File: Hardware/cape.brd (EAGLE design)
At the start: 105 x 118 mm, 99 parts, among them IC1 RT7258, IC2 RT7258, IC3 74HC125, J1 JST-BM07B-GHS-TBT, J10 JST-BM07B-GHS-TBT, J11 JST-BM07B-GHS-TBT, J12 JST-BM07B-GHS-TBT, J13 JST-BM07B-GHS-TBT, J14 JST-BM07B-GHS-TBT, J15 JST-BM07B-GHS-TBT, J16 JST-BM07B-GHS-TBT, J17 JST-BM07B-GHS-TBT, J18 JST-BM07B-GHS-TBT, J19 JST-BM07B-GHS-TBT, J2 JST-BM07B-GHS-TBT, J20 JST-BM07B-GHS-TBT, J21 JST-BM07B-GHS-TBT, J22 JST-BM07B-GHS-TBT, J23 JST-BM07B-GHS-TBT, J24 JST-BM07B-GHS-TBT, J25 JST-BM07B-GHS-TBT, J26 JST-BM07B-GHS-TBT, J27 JST-BM07B-GHS-TBT, J28 JST-BM07B-GHS-TBT, J29 JST-BM07B-GHS-TBT, J3 JST-BM07B-GHS-TBT, J30 JST-BM07B-GHS-TBT, J31 JST-BM07B-GHS-TBT, J32 JST-BM07B-GHS-TBT, J4 JST-BM07B-GHS-TBT, J5 JST-BM07B-GHS-TBT, J6 JST-BM07B-GHS-TBT, J7 JST-BM07B-GHS-TBT, J8 JST-BM07B-GHS-TBT, J9 JST-BM07B-GHS-TBT, Q1 FDS6670, Q2 FDS6670, X1 RJ45-6L2-B, X2 RJ45-6L2-B

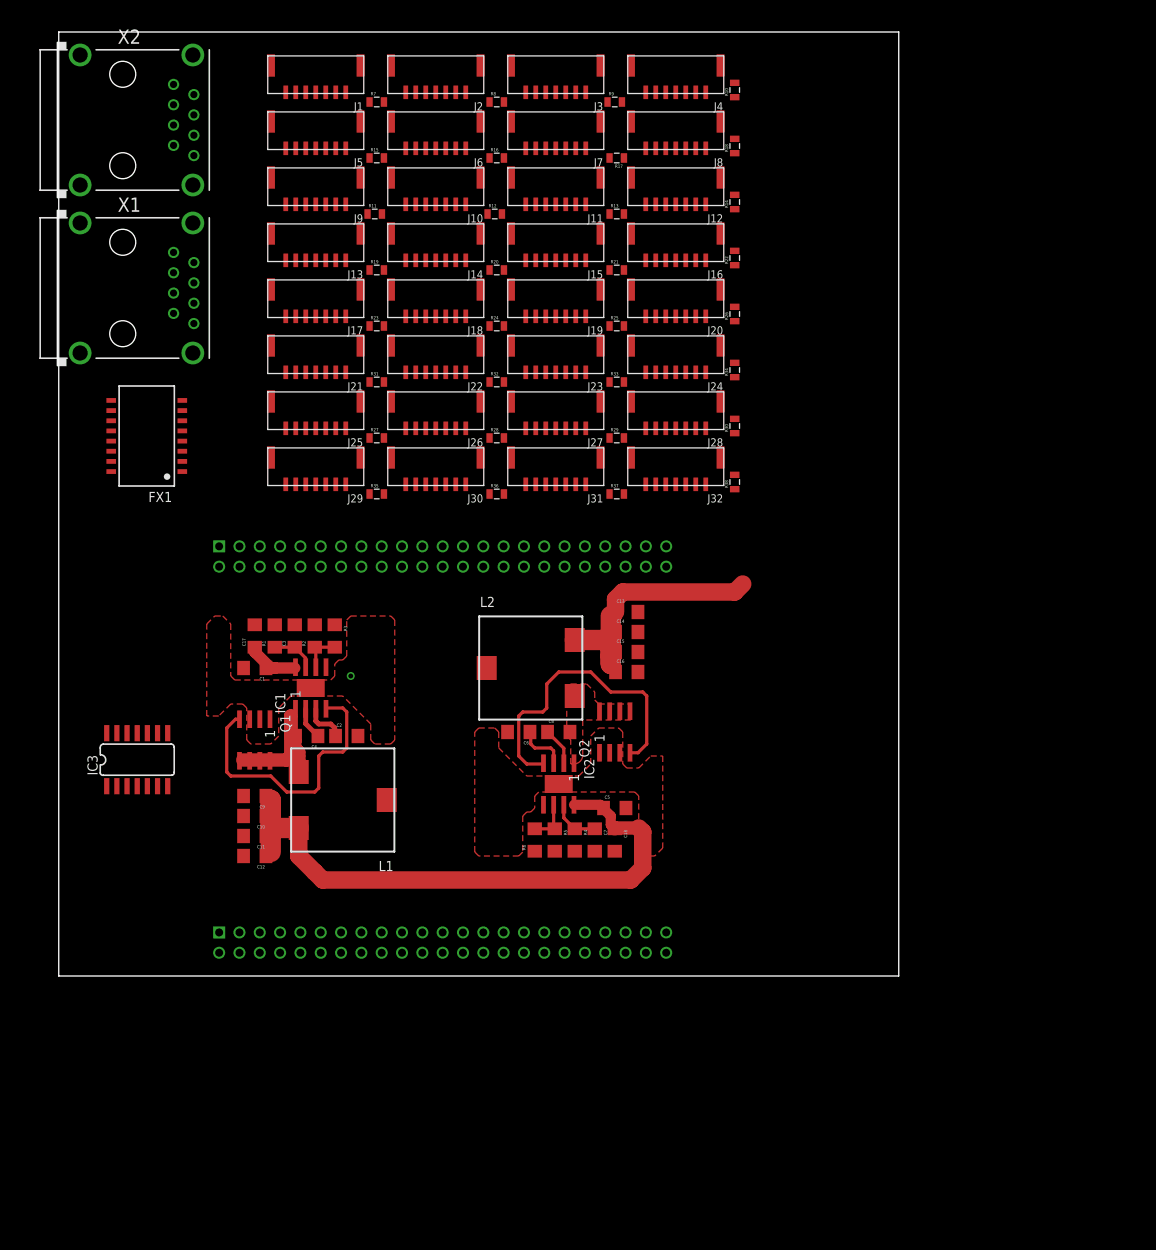
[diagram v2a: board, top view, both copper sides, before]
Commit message: routing and pinmapping
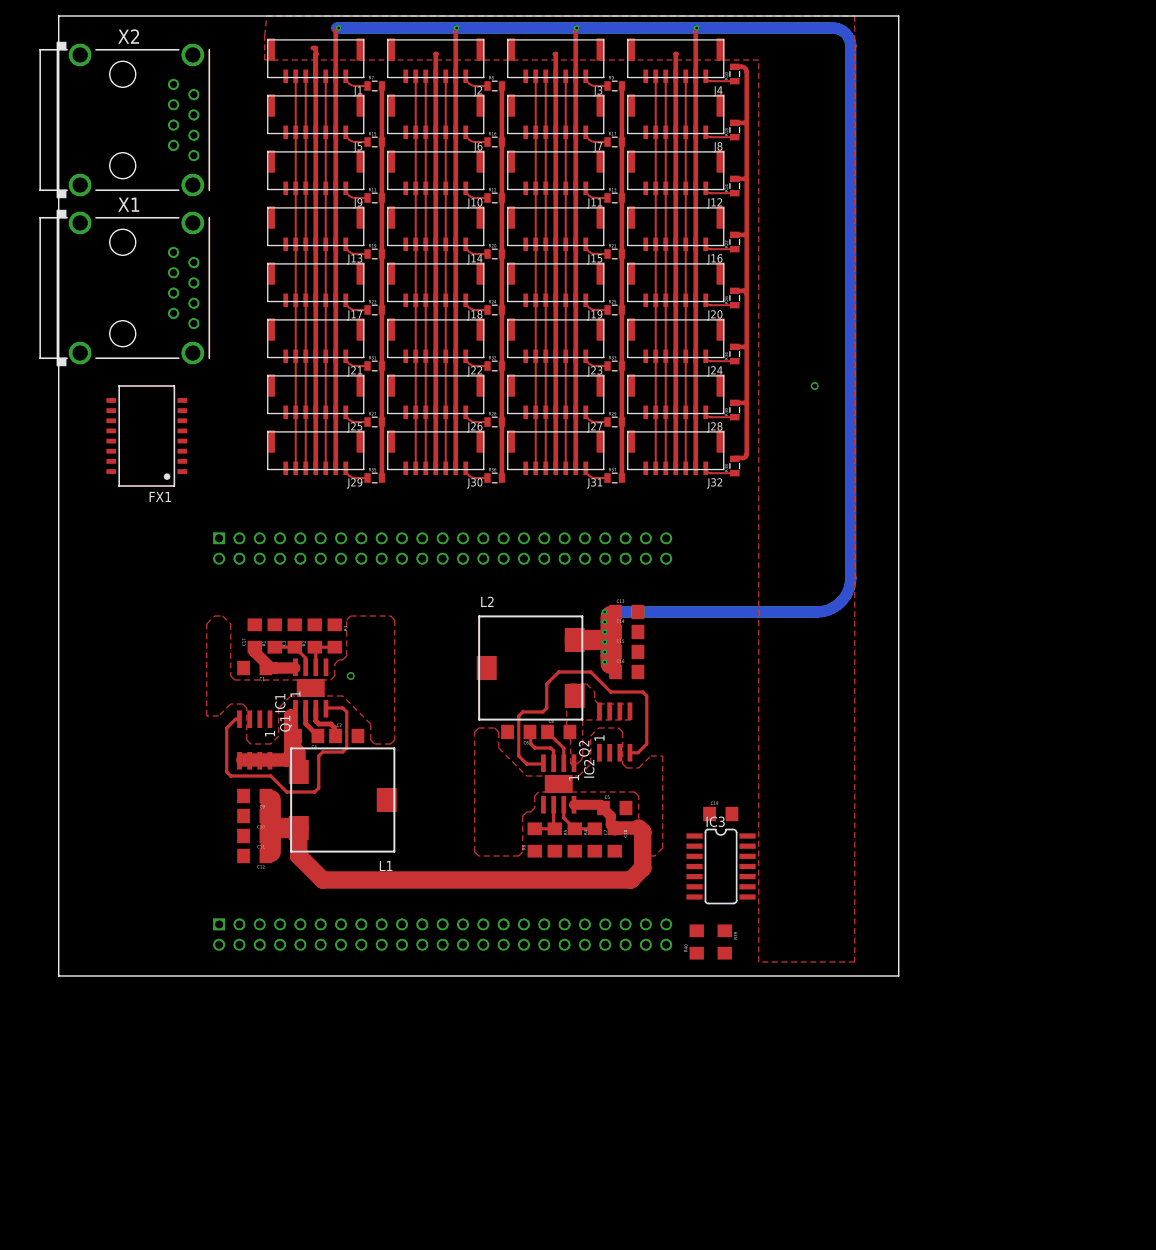
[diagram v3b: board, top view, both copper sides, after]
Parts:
- added C19: 1uF, SparkFun-Capacitors:1206
- added R39, R40: 10k, SparkFun-Passives:1206
- moved IC3 74.6 mm to (80.2, 17.5), turned to 270 degrees
- moved R13 2.02 mm to (69.5, 97.2)
- moved R15 2.02 mm to (39.5, 104.2)
- moved R16 2.02 mm to (54.5, 104.2)
- moved R17 2.02 mm to (69.5, 104.2), turned to 0 degrees
- moved R19 2.02 mm to (39.5, 90.2)
- moved R20 2.02 mm to (54.5, 90.2)
- moved R21 2.02 mm to (69.5, 90.2)
- moved R23 2.02 mm to (39.5, 83.2)
- moved R24 2.02 mm to (54.5, 83.2)
- moved R25 2.02 mm to (69.5, 83.2)
- moved R27 2.02 mm to (39.5, 69.2)
- moved R28 2.02 mm to (54.5, 69.2)
- moved R29 2.02 mm to (69.5, 69.2)
- moved R31 2.02 mm to (39.5, 76.2)
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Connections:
- removed net N$6: IC3.12
- new net SDI-2: J2.1, U$1.67
- net DC: now also IC3.6
- net DC_RAW: now also U$1.9
- net GND: now also C19.1, IC3.12, R40.1
- net RST: now also IC3.8
- net RST_RAW: now also R39.1, R40.2, U$1.46
- net SCL: now also IC3.3
- net SCL_RAW: now also U$1.45
- net SDI-1: now also U$1.68; no longer J2.1
- net SDI-10: now also U$1.72
- net SDI-11: now also U$1.70
- net SDI-12: now also U$1.87
- net SDI-13: now also U$1.19
- net SDI-14: now also U$1.13
- net SDI-15: now also U$1.14
- net SDI-16: now also U$1.17
- net SDI-17: now also U$1.57
- net SDI-18: now also U$1.59
- net SDI-19: now also U$1.12
- net SDI-20: now also U$1.11
- net SDI-21: now also U$1.16
- net SDI-22: now also U$1.15
- net SDI-23: now also U$1.61
- net SDI-24: now also U$1.69
- net SDI-25: now also U$1.60
- net SDI-26: now also U$1.62
- net SDI-27: now also U$1.58
- net SDI-28: now also U$1.26
- net SDI-29: now also U$1.18
- net SDI-3: now also U$1.64
- net SDI-30: now also U$1.7
- net SDI-31: now also U$1.8
- net SDI-32: now also U$1.10
- net SDI-4: now also U$1.63
- net SDI-5: now also U$1.88
- net SDI-6: now also U$1.35
- net SDI-7: now also U$1.33
- net SDI-8: now also U$1.31
- net SDI-9: now also U$1.32
- net VCC3V3: now also C19.2, IC3.14, R39.2
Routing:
- net VCC3V3: track 36.2 -> 409.8 mm, vias 0 -> 10
- net GND: track 0.00 -> 211.6 mm, vias 1 -> 2
- net VCC5V: track 83.1 -> 287.3 mm
- net SCL: track 0.00 -> 196.0 mm
- net RST: track 0.00 -> 196.0 mm
- net DC: track 0.00 -> 196.0 mm
- net LED-8: track 0.00 -> 3.88 mm
- net LED-4: track 0.00 -> 3.88 mm
- net LED-32: track 0.00 -> 3.88 mm
- net LED-28: track 0.00 -> 3.88 mm
- net LED-24: track 0.00 -> 3.88 mm
- net LED-20: track 0.00 -> 3.88 mm
- net LED-16: track 0.00 -> 3.88 mm
- net LED-12: track 0.00 -> 3.88 mm
- net LED-30: track 0.00 -> 3.23 mm
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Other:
- board size 105 x 118 mm -> 105 x 120 mm

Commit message: Updated cape schematic and library, added datasheets
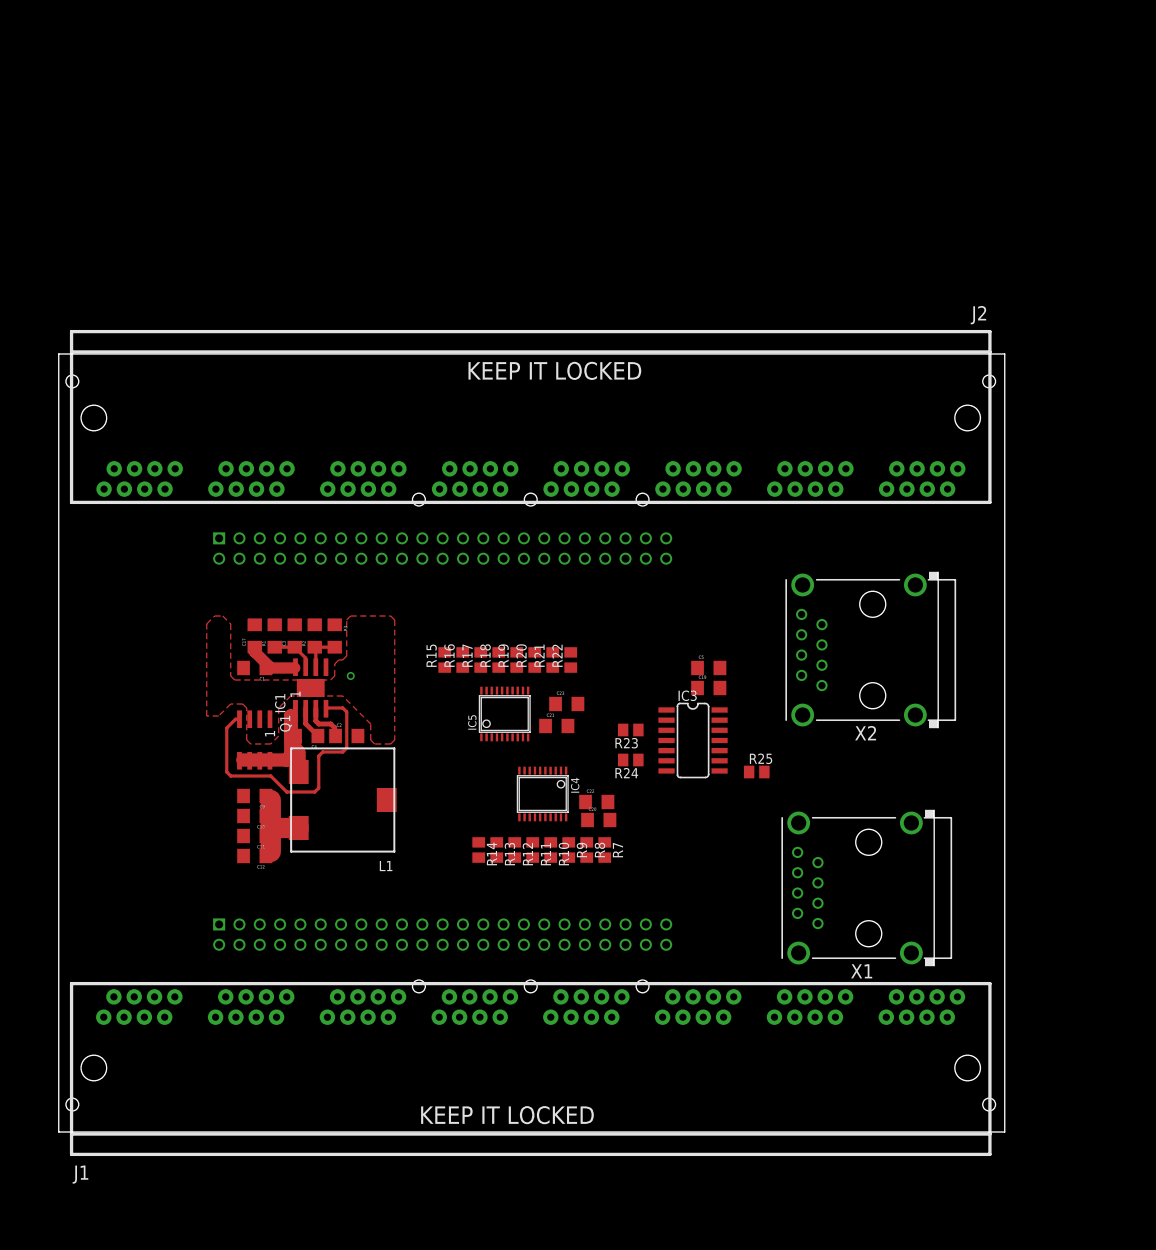
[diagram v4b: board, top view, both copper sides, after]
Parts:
- removed C13, C14: 22uF, SparkFun-Capacitors:1206
- removed C15, C16: 47uF, SparkFun-Capacitors:1206
- removed C18: 10uF, SparkFun-Capacitors:1206
- removed C6, C7, C8: 1uF, SparkFun-Capacitors:1206
- removed FX1: TG110-E055N5, halo-electronics:N5
- removed IC2: RT7258, TotU:SOP08-PAD
- removed J10, J11, J12, J13, J14, J15, J16, J17, J18, J19, J20, J21, J22, J23, J24, J25, J26, J27, J28, J29, J3, J30, J31, J32, J4, J5, J6, J7, J8, J9: JST-BM07B-GHS-TBT, TotU:JST-BM07B-GHS-TBT
- removed L2: MURATA_INDUCTOR_3900, TotU:MURATA_INDUCTOR_3900
- removed Q2: FDS6670, TotU:SOP08
- removed R26, R27, R28, R29, R30, R31, R32, R33, R34, R35, R36, R37, R38: (no value), SparkFun-Passives:0805
- removed R39, R40: 10k, SparkFun-Passives:1206
- removed R4: 100k, SparkFun-Passives:1206
- removed R5: 62k, SparkFun-Passives:1206
- removed R6: 20k, SparkFun-Passives:1206
- added C20, C21: 1uF, SparkFun-Capacitors:1206
- added C22, C23: 10uF, SparkFun-Capacitors:1206
- added IC4, IC5: 74VHC541, cape:TSSOP20
- C5: value 22uF -> 10uF
- J1, J2: value JST-BM07B-GHS-TBT -> FCI-10118064-5001310LF; device TotU:JST-BM07B-GHS-TBT -> cape:FCI-10118064-5001310LF
- R10, R11, R12, R13, R14, R15, R16, R17, R18, R19, R20, R21, R22, R23, R24, R25, R7, R8, R9: device SparkFun-Passives:0805 -> resistor:M0805
- moved J1 129.5 mm to (59.0, -11.5), turned to 0 degrees
- moved X1 119.7 mm to (101.2, 11.0), turned to 90 degrees
- moved X2 114.8 mm to (101.8, 40.8), turned to 90 degrees
- moved R7 99.7 mm to (68.2, 15.8), turned to 270 degrees
- moved R10 99.7 mm to (61.5, 15.8), turned to 270 degrees
- moved R8 96.2 mm to (66.0, 15.8), turned to 270 degrees
- moved R9 95.7 mm to (63.8, 15.8), turned to 270 degrees
- moved R14 89.0 mm to (52.5, 15.8), turned to 270 degrees
- moved R11 83.9 mm to (59.2, 15.8), turned to 270 degrees
- moved R13 82.8 mm to (54.8, 15.8), turned to 270 degrees
- moved R12 81.5 mm to (57.0, 15.8), turned to 270 degrees
- moved R18 72.5 mm to (55.0, 39.5)
- moved R17 66.9 mm to (52.8, 39.5), turned to 90 degrees
- moved R15 65.3 mm to (48.2, 39.5), turned to 90 degrees
- moved R16 64.9 mm to (50.5, 39.5), turned to 90 degrees
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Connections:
- removed net LED-1: J1.7, R7.1
- removed net LED-10: J10.7, R12.1
- removed net LED-11: J11.7, R13.1
- removed net LED-12: J12.7, R14.1
- removed net LED-13: J13.7, R19.1
- removed net LED-14: J14.7, R20.1
- removed net LED-15: J15.7, R21.1
- removed net LED-16: J16.7, R22.1
- removed net LED-17: J17.7, R23.1
- removed net LED-18: J18.7, R24.1
- removed net LED-19: J19.7, R25.1
- removed net LED-2: J2.7, R8.1
- removed net LED-20: J20.7, R26.1
- removed net LED-21: J21.7, R31.1
- removed net LED-22: J22.7, R32.1
- removed net LED-23: J23.7, R33.1
- removed net LED-24: J24.7, R34.1
- removed net LED-25: J25.7, R27.1
- removed net LED-26: J26.7, R28.1
- removed net LED-27: J27.7, R29.1
- removed net LED-28: J28.7, R30.1
- removed net LED-29: J29.7, R35.1
- removed net LED-3: J3.7, R9.1
- removed net LED-30: J30.7, R36.1
- removed net LED-31: J31.7, R37.1
- removed net LED-32: J32.7, R38.1
- removed net LED-4: J4.7, R10.1
- removed net LED-5: J5.7, R15.1
- removed net LED-6: J6.7, R16.1
- removed net LED-7: J7.7, R17.1
- removed net LED-8: J8.7, R18.1
- removed net LED-9: J9.7, R11.1
- removed net N$10: C7.1, IC2.7, R4.1
- removed net N$11: C8.1, IC2.2
- removed net N$12: C8.2, IC2.1, L2.1, Q2.5, Q2.6, Q2.7, Q2.8
- removed net N$14: IC2.6, R5.1, R6.2
- removed net N$15: IC2.4, Q2.4
- removed net N$9: C6.1, IC2.3
- removed net RD+: FX1.3, X2.3
- removed net RD-: FX1.1, X2.6
- removed net SCL: IC3.3, J1.2, J10.2, J11.2, J12.2, J13.2, J14.2, J15.2, J16.2, J17.2, J18.2, J19.2, J2.2, J20.2, J21.2, J22.2, J23.2, J24.2, J25.2, J26.2, J27.2, J28.2, J29.2, J3.2, J30.2, J31.2, J32.2, J4.2, J5.2, J6.2, J7.2, J8.2, J9.2
- removed net SDI-1: J1.1, U$1.68
- removed net SDI-10: J10.1, U$1.72
- removed net SDI-11: J11.1, U$1.70
- removed net SDI-12: J12.1, U$1.87
- removed net SDI-13: J13.1, U$1.19
- removed net SDI-14: J14.1, U$1.13
- removed net SDI-15: J15.1, U$1.14
- removed net SDI-16: J16.1, U$1.17
- removed net SDI-17: J17.1, U$1.57
- removed net SDI-18: J18.1, U$1.59
- removed net SDI-19: J19.1, U$1.12
- removed net SDI-2: J2.1, U$1.67
- removed net SDI-20: J20.1, U$1.11
- removed net SDI-21: J21.1, U$1.16
- removed net SDI-22: J22.1, U$1.15
- removed net SDI-23: J23.1, U$1.61
- removed net SDI-24: J24.1, U$1.69
- removed net SDI-25: J25.1, U$1.60
- removed net SDI-26: J26.1, U$1.62
- removed net SDI-27: J27.1, U$1.58
- removed net SDI-28: J28.1, U$1.26
- removed net SDI-29: J29.1, U$1.18
- removed net SDI-3: J3.1, U$1.64
- removed net SDI-30: J30.1, U$1.7
- removed net SDI-31: J31.1, U$1.8
- removed net SDI-32: J32.1, U$1.10
- removed net SDI-4: J4.1, U$1.63
- removed net SDI-5: J5.1, U$1.88
- removed net SDI-6: J6.1, U$1.35
- removed net SDI-7: J7.1, U$1.33
- removed net SDI-8: J8.1, U$1.31
- removed net SDI-9: J9.1, U$1.32
- removed net TD+: FX1.8, X2.1
- removed net TD-: FX1.6, X2.2
- new net AD0: IC4.9, U$1.25
- new net AD1: IC4.8, U$1.24
- new net AD10: IC5.7, U$1.14
- new net AD11: IC5.6, U$1.17
- new net AD12: IC5.5, U$1.12
- new net AD13: IC5.4, U$1.11
- new net AD14: IC5.3, U$1.16
- new net AD15: IC5.2, U$1.15
- new net AD2: IC4.7, U$1.5
- new net AD3: IC4.6, U$1.6
- new net AD4: IC4.5, U$1.23
- new net AD5: IC4.4, U$1.22
- new net AD6: IC4.3, U$1.3
- new net AD7: IC4.2, U$1.4
- new net AD8: IC5.9, U$1.19
- new net AD9: IC5.8, U$1.13
- new net BKL0: J1.A6
- new net BLK1: J1.B6
- new net BLK10: J2.C6
- new net BLK11: J2.D6
- new net BLK12: J2.E6
- new net BLK13: J2.F6
- new net BLK14: J2.G6
- new net BLK15: J2.H6
- new net BLK2: J1.C6
- new net BLK3: J1.D6
- new net BLK4: J1.E6
- new net BLK5: J1.F6
- new net BLK6: J1.G6
- new net BLK7: J1.H6
- new net BLK8: J2.A6
- new net BLK9: J2.B6
- new net DATA0: J1.A1, R14.2
- new net DATA1: J1.B1, R13.2
- new net DATA10: J2.C1, R20.2
- new net DATA11: J2.D1, R19.2
- new net DATA12: J2.E1, R18.2
- new net DATA13: J2.F1, R17.2
- new net DATA14: J2.G1, R16.2
- new net DATA15: J2.H1, R15.2
- new net DATA2: J1.C1, R12.2
- new net DATA3: J1.D1, R11.2
- new net DATA4: J1.E1, R10.2
- new net DATA5: J1.F1, R9.2
- new net DATA6: J1.G1, R8.2
- new net DATA7: J1.H1, R7.2
- new net DATA8: J2.A1, R22.2
- new net DATA9: J2.B1, R21.2
- new net N$13: IC4.16, R9.1
- new net N$16: IC4.15, R10.1
- new net N$17: IC4.14, R11.1
- new net N$18: IC4.13, R12.1
- new net N$19: IC4.12, R13.1
- new net N$20: IC4.11, R14.1
- new net N$21: IC5.18, R15.1
- new net N$22: IC5.17, R16.1
- new net N$23: IC5.16, R17.1
- new net N$24: IC5.15, R18.1
- new net N$25: IC5.14, R19.1
- new net N$26: IC5.13, R20.1
- new net N$27: IC5.12, R21.1
- new net N$28: IC5.11, R22.1
- new net N$29: IC3.8, R25.1
- new net N$30: IC3.6, R24.1
- new net N$31: IC3.3, R23.1
- new net N$5: IC4.18, R7.1
- new net N$6: IC4.17, R8.1
- new net SCK: J1.A8, J1.B8, J1.C8, J1.D8, J1.E8, J1.F8, J1.G8, J1.H8, J2.A8, J2.B8, J2.C8, J2.D8, J2.E8, J2.F8, J2.G8, J2.H8, R23.2
- net DC: now also J1.A4, J1.B4, J1.C4, J1.D4, J1.E4, J1.F4, J1.G4, J1.H4, J2.A4, J2.B4, J2.C4, J2.D4, J2.E4, J2.F4, J2.G4, J2.H4, R24.2; no longer IC3.6, J1.3, J10.3, J11.3, J12.3, J13.3, J14.3, J15.3, J16.3, J17.3, J18.3, J19.3, J2.3, J20.3, J21.3, J22.3, J23.3, J24.3, J25.3, J26.3, J27.3, J28.3, J29.3, J3.3, J30.3, J31.3, J32.3, J4.3, J5.3, J6.3, J7.3, J8.3, J9.3
- net DC_RAW: now also U$1.26; no longer U$1.9
- net GND: now also C20.2, C21.2, C22.2, C23.2, C5.1, IC4.1, IC4.10, IC4.19, IC5.1, IC5.10, IC5.19, J1.A2, J1.A7, J1.B2, J1.B7, J1.C2, J1.C7, J1.D2, J1.D7, J1.E2, J1.E7, J1.F2, J1.F7, J1.G2, J1.G7, J1.H2, J1.H7, J2.A2, J2.A7, J2.B2, J2.B7, J2.C2, J2.C7, J2.D2, J2.D7, J2.E2, J2.E7, J2.F2, J2.F7, J2.G2, J2.G7, J2.H2, J2.H7; no longer C13.2, C14.2, C15.2, C16.2, C18.2, C5.2, C6.2, C7.2, FX1.15, IC2.5, IC2.EXP, J1.4, J10.4, J11.4, J12.4, J13.4, J14.4, J15.4, J16.4, J17.4, J18.4, J19.4, J2.4, J20.4, J21.4, J22.4, J23.4, J24.4, J25.4, J26.4, J27.4, J28.4, J29.4, J3.4, J30.4, J31.4, J32.4, J4.4, J5.4, J6.4, J7.4, J8.4, J9.4, Q2.1, Q2.2, Q2.3, R40.1, R6.1
- net RST: now also J1.A5, J1.B5, J1.C5, J1.D5, J1.E5, J1.F5, J1.G5, J1.H5, J2.A5, J2.B5, J2.C5, J2.D5, J2.E5, J2.F5, J2.G5, J2.H5, R25.2; no longer IC3.8, J1.5, J10.5, J11.5, J12.5, J13.5, J14.5, J15.5, J16.5, J17.5, J18.5, J19.5, J2.5, J20.5, J21.5, J22.5, J23.5, J24.5, J25.5, J26.5, J27.5, J28.5, J29.5, J3.5, J30.5, J31.5, J32.5, J4.5, J5.5, J6.5, J7.5, J8.5, J9.5
- net RST_RAW: now also U$1.20; no longer R39.1, R40.2, U$1.46
- net RX+: now also X2.3; no longer FX1.14
- net RX-: now also X2.6; no longer FX1.16
- net SCL_RAW: now also U$1.10; no longer U$1.45
- net TX+: now also X2.1; no longer FX1.9
- net TX-: now also X2.2; no longer FX1.11
- net VCC3V3: now also C20.1, C21.1, C22.1, C23.1, C5.2, IC4.20, IC5.20, J1.A3, J1.B3, J1.C3, J1.D3, J1.E3, J1.F3, J1.G3, J1.H3, J2.A3, J2.B3, J2.C3, J2.D3, J2.E3, J2.F3, J2.G3, J2.H3, U$1.50; no longer C13.1, C14.1, C15.1, C16.1, J1.6, J10.6, J11.6, J12.6, J13.6, J14.6, J15.6, J16.6, J17.6, J18.6, J19.6, J2.6, J20.6, J21.6, J22.6, J23.6, J24.6, J25.6, J26.6, J27.6, J28.6, J29.6, J3.6, J30.6, J31.6, J32.6, J4.6, J5.6, J6.6, J7.6, J8.6, J9.6, L2.2, R39.2, R5.2
- net VCC5V: no longer C18.1, C5.1, IC2.8, R10.2, R11.2, R12.2, R13.2, R14.2, R15.2, R16.2, R17.2, R18.2, R19.2, R20.2, R21.2, R22.2, R23.2, R24.2, R25.2, R26.2, R27.2, R28.2, R29.2, R30.2, R31.2, R32.2, R33.2, R34.2, R35.2, R36.2, R37.2, R38.2, R4.2, R7.2, R8.2, R9.2
- net VDD_3V3EXP: no longer U$1.50
- net VIN: no longer FX1.10
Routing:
- net VCC3V3: track 409.8 -> 0.00 mm, vias 10 -> 0
- net VCC5V: track 287.3 -> 15.9 mm
- net GND: track 211.6 -> 0.00 mm, vias 2 -> 1
- net SCL: track 196.0 -> 0.00 mm
- net RST: track 196.0 -> 0.00 mm
- net DC: track 196.0 -> 0.00 mm
- net N$15: track 38.4 -> 0.00 mm
- net N$9: track 6.30 -> 0.00 mm
- net N$10: track 6.07 -> 0.00 mm
- net N$14: track 5.56 -> 0.00 mm
- net N$11: track 4.74 -> 0.00 mm
- net LED-8: track 3.88 -> 0.00 mm
- net LED-4: track 3.88 -> 0.00 mm
- net LED-32: track 3.88 -> 0.00 mm
- net LED-28: track 3.88 -> 0.00 mm
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- removed copper zone on layer 1, net N$12
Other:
- board size 105 x 120 mm -> 118.2 x 97.2 mm
